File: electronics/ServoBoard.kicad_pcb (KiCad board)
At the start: 2 copper layers, 8 parts, among them K1 Left Servo, K2 Right Servo, P1 Pi GPIO Header, P2 CONN_2, U1 7805

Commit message: Gerber Files
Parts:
- added P3: CONNECTOR, 1pin, F.Cu at (40.6, 67.3)
- added P4: CONNECTOR, 1pin, F.Cu at (95.2, 111.8)
- added P5: CONNECTOR, 1pin, F.Cu at (40.6, 111.8)
- P2: footprint 2PIN_6mm -> PINHEAD1-2
- moved R1 36.9 mm to (40.6, 99.1), turned to 90 degrees
- moved C1 33.1 mm to (63.5, 96.5), turned to 270 degrees
- moved D1 23.3 mm to (40.6, 91.4), turned to 90 degrees
- moved K2 21.8 mm to (59.7, 110.5)
- moved K1 18.5 mm to (49.5, 110.5)
- moved P2 18.0 mm to (40.6, 85.1)
- moved P1 5.68 mm to (68.6, 68.6)
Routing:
- net N-0000033: track 0.00 -> 57.8 mm, vias 0 -> 4
- net N-000006: track 0.00 -> 42.7 mm
- net N-000008: track 0.00 -> 40.6 mm
- added copper zone on B.Cu, net +6V
- added copper zone on F.Cu, net GND
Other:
- board outline added: 59.7 x 49.5 mm
- board text added: "TurtleBot ServoBoard v0.1"

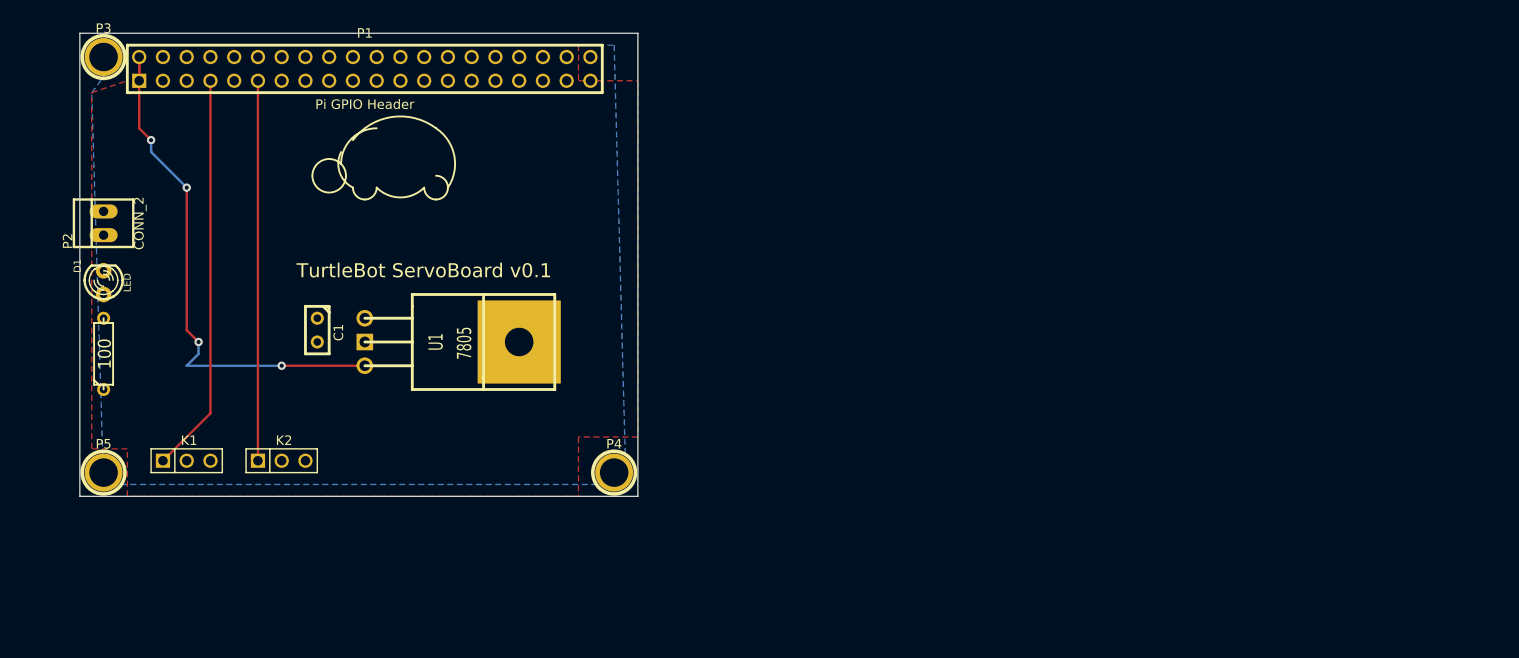
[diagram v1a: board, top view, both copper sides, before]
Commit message: Updated to be 5.6 x 6.5cm in width/length.
Moved pins to be over correct location.
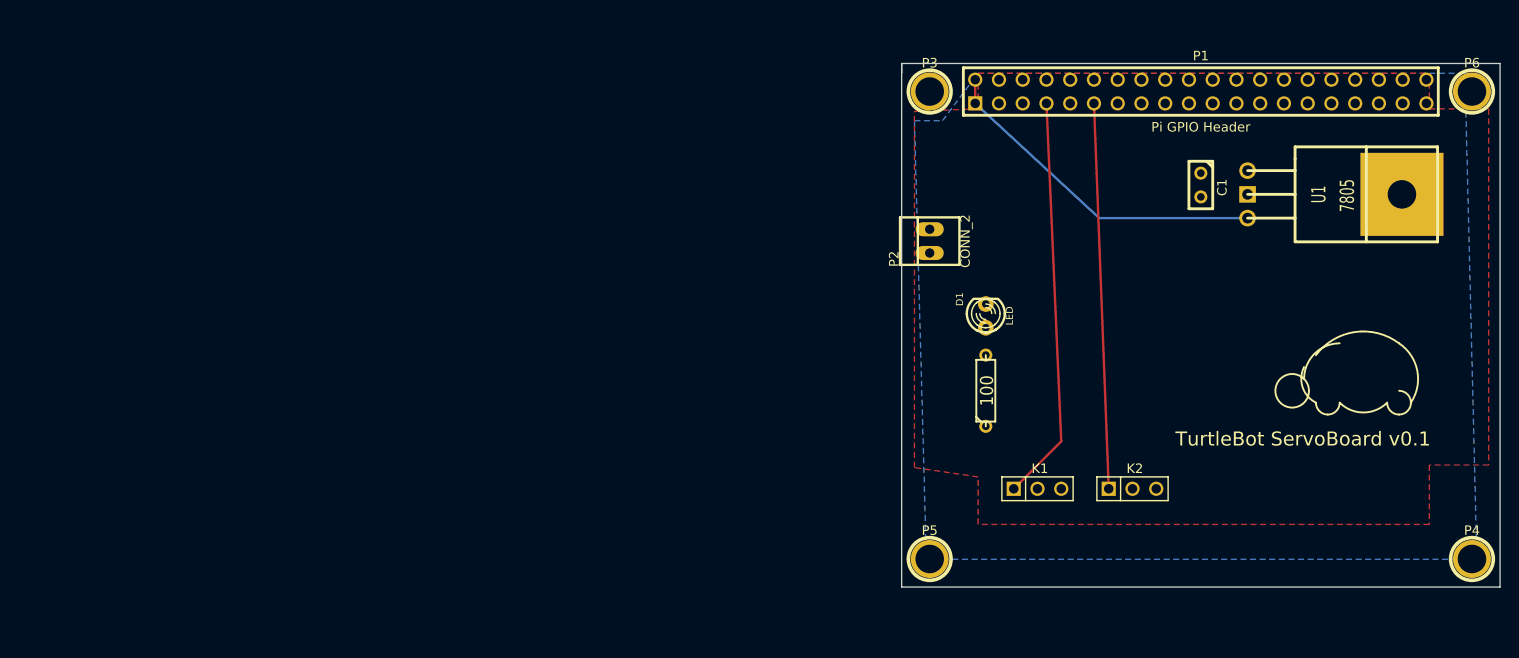
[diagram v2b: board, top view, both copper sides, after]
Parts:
- added P6: CONNECTOR, 1pin, F.Cu at (187.0, 71.0)
- moved C1 95.8 mm to (158.0, 81.0)
- moved U1 95.7 mm to (163.0, 82.0)
- moved R1 94.4 mm to (135.0, 103.0)
- moved D1 94.4 mm to (135.0, 95.0)
- moved P4 92.2 mm to (187.0, 121.0)
- moved K1 91.0 mm to (140.5, 113.5)
- moved K2 91.0 mm to (150.7, 113.5)
- moved P1 89.5 mm to (158.0, 71.0)
- moved P5 88.8 mm to (129.0, 121.0)
- moved P3 88.4 mm to (129.0, 71.0)
- moved P2 88.4 mm to (129.0, 87.0)
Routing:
- net N-0000033: track 57.8 -> 36.5 mm, vias 4 -> 0
- net N-000006: track 42.7 -> 43.4 mm
- net N-000008: track 40.6 -> 41.3 mm
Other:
- board size 59.7 x 49.5 mm -> 64 x 56 mm
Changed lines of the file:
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@@
     (links 16)
     (no_connects 1)
-    (area 35.179 63.373 100.711 115.443)
+    (area 123.539 66.29084 193.461 124.683)
     (thickness 1.6)
-    (drawings 16)
-    (tracks 18)
+    (drawings 18)
+    (tracks 6)
     (zones 0)
-    (modules 11)
+    (modules 12)
     (nets 7)
   )
@@
   )
   (module R3 (layer F.Cu)
-    (at 40.64 99.06 90)
+    (at 135 103 90)
     (descr "Resitance 3 pas")
     (tags R)
@@
   )
   (module PIN_ARRAY_20X2 (layer F.Cu)
-    (at 68.58 68.58)
+    (at 158 71)
     (descr "Double rangee de contacts 2 x 12 pins")
     (tags CONN)
@@
   )
   (module LM78XX (layer F.Cu)
-    (at 68.58 97.79)
+    (at 163 82)
     (descr "Regulateur TO220 serie LM78xx")
     (tags "TR TO220")
@@
   )
   (module LED-3MM (layer F.Cu)
-    (at 40.64 91.44 90)
+    (at 135 95 90)
     (descr "LED 3mm - Lead pitch 100mil (2,54mm)")
     (tags "LED led 3mm 3MM 100mil 2,54mm")
@@
   )
   (module C1 (layer F.Cu)
-    (at 63.5 96.52 270)
+    (at 158 81 270)
     (descr "Condensateur e = 1 pas")
     (tags C)
@@
   )
   (module PIN_ARRAY_3X1 (layer F.Cu)
-    (at 49.53 110.49)
+    (at 140.53 113.49)
     (descr "Connecteur 3 pins")
     (tags "CONN DEV")
@@
   )
   (module PIN_ARRAY_3X1 (layer F.Cu)
-    (at 59.69 110.49)
+    (at 150.69 113.49)
     (descr "Connecteur 3 pins")
     (tags "CONN DEV")
@@
   )
   (module 1pin (layer F.Cu)
-    (at 40.64 67.31)
+    (at 129 71)
     (descr "module 1 pin (ou trou mecanique de percage)")
     (tags DEV)
@@
   )
   (module 1pin (layer F.Cu)
-    (at 40.64 111.76)
+    (at 129 121)
     (descr "module 1 pin (ou trou mecanique de percage)")
     (tags DEV)
@@
   )
   (module 1pin (layer F.Cu)
-    (at 95.25 111.76)
+    (at 187 121)
     (descr "module 1 pin (ou trou mecanique de percage)")
     (tags DEV)
@@
   )
   (module PINHEAD1-2 (layer F.Cu)
-    (at 40.64 85.09 90)
+    (at 129 87 90)
     (attr virtual)
     (fp_text reference P2 (at -1.905 -3.81 90) (layer F.SilkS)
@@
     )
   )
-  (gr_arc (start 68.58 78.74) (end 67.31 81.28) (angle 90) (layer F.SilkS) (width 0.2))
-  (gr_arc (start 68.58 81.28) (end 68.58 82.55) (angle 90) (layer F.SilkS) (width 0.2))
-  (gr_arc (start 68.58 81.28) (end 69.85 81.28) (angle 90) (layer F.SilkS) (width 0.2))
-  (gr_arc (start 72.39 78.74) (end 74.93 81.28) (angle 90) (layer F.SilkS) (width 0.2))
-  (gr_arc (start 76.2 81.28) (end 76.2 82.55) (angle 90) (layer F.SilkS) (width 0.2))
-  (gr_arc (start 76.2 81.28) (end 77.47 81.28) (angle 90) (layer F.SilkS) (width 0.2))
-  (gr_arc (start 76.2 81.28) (end 76.2 80.01) (angle 90) (layer F.SilkS) (width 0.2))
-  (gr_arc (start 73.66 78.74) (end 76.2 74.93) (angle 90) (layer F.SilkS) (width 0.2))
-  (gr_arc (start 69.85 78.74) (end 66.04 78.74) (angle 90) (layer F.SilkS) (width 0.2))
-  (gr_arc (start 72.39 80.01) (end 67.31 76.2) (angle 90) (layer F.SilkS) (width 0.2))
-  (gr_circle (center 64.77 80.01) (end 66.04 81.28) (layer F.SilkS) (width 0.2))
-  (gr_text "TurtleBot ServoBoard v0.1" (at 74.93 90.17) (layer F.SilkS)
+  (module 1pin (layer F.Cu)
+    (at 187 71)
+    (descr "module 1 pin (ou trou mecanique de percage)")
+    (tags DEV)
+    (fp_text reference P6 (at 0 -3.048) (layer F.SilkS)
+      (effects (font (size 1.016 1.016) (thickness 0.254)))
+    )
+    (fp_text value CONNECTOR (at 0 2.794) (layer F.SilkS) hide
+      (effects (font (size 1.016 1.016) (thickness 0.254)))
+    )
+    (fp_circle (center 0 0) (end 0 -2.286) (layer F.SilkS) (width 0.381))
+    (pad 1 thru_hole circle (at 0 0) (size 4.064 4.064) (drill 3.048)
+      (layers *.Cu *.Mask F.SilkS)
+    )
+  )
+  (gr_line (start 190 124) (end 126 124) (angle 90) (layer Edge.Cuts) (width 0.1))
+  (gr_line (start 190 68) (end 126 68) (angle 90) (layer Edge.Cuts) (width 0.1))
+  (gr_line (start 190 124) (end 190 68) (angle 90) (layer Edge.Cuts) (width 0.1))
+  (gr_line (start 126 69) (end 126 68) (angle 90) (layer Edge.Cuts) (width 0.1))
+  (gr_line (start 126 68) (end 126 69) (angle 90) (layer Edge.Cuts) (width 0.1))
+  (gr_line (start 126 124) (end 126 69) (angle 90) (layer Edge.Cuts) (width 0.1))
+  (gr_arc (start 171.58 101.74) (end 170.31 104.28) (angle 90) (layer F.SilkS) (width 0.2))
+  (gr_arc (start 171.58 104.28) (end 171.58 105.55) (angle 90) (layer F.SilkS) (width 0.2))
+  (gr_arc (start 171.58 104.28) (end 172.85 104.28) (angle 90) (layer F.SilkS) (width 0.2))
+  (gr_arc (start 175.39 101.74) (end 177.93 104.28) (angle 90) (layer F.SilkS) (width 0.2))
+  (gr_arc (start 179.2 104.28) (end 179.2 105.55) (angle 90) (layer F.SilkS) (width 0.2))
+  (gr_arc (start 179.2 104.28) (end 180.47 104.28) (angle 90) (layer F.SilkS) (width 0.2))
+  (gr_arc (start 179.2 104.28) (end 179.2 103.01) (angle 90) (layer F.SilkS) (width 0.2))
+  (gr_arc (start 176.66 101.74) (end 179.2 97.93) (angle 90) (layer F.SilkS) (width 0.2))
+  (gr_arc (start 172.85 101.74) (end 169.04 101.74) (angle 90) (layer F.SilkS) (width 0.2))
+  (gr_arc (start 175.39 103.01) (end 170.31 99.2) (angle 90) (layer F.SilkS) (width 0.2))
+  (gr_circle (center 167.77 103.01) (end 169.04 104.28) (layer F.SilkS) (width 0.2))
+  (gr_text "TurtleBot ServoBoard v0.1" (at 168.93 108.17) (layer F.SilkS)
     (effects (font (size 1.5 1.5) (thickness 0.3)))
   )
-  (gr_line (start 38.1 114.3) (end 38.1 64.77) (angle 90) (layer Edge.Cuts) (width 0.1))
-  (gr_line (start 97.79 114.3) (end 38.1 114.3) (angle 90) (layer Edge.Cuts) (width 0.1))
-  (gr_line (start 97.79 64.77) (end 97.79 114.3) (angle 90) (layer Edge.Cuts) (width 0.1))
-  (gr_line (start 38.1 64.77) (end 97.79 64.77) (angle 90) (layer Edge.Cuts) (width 0.1))
-  (segment (start 44.45 69.85) (end 44.45 67.31) (width 0.254) (layer F.Cu) (net 4))
-  (segment (start 68.58 100.33) (end 59.69 100.33) (width 0.254) (layer F.Cu) (net 4))
-  (segment (start 44.45 74.93) (end 44.45 67.31) (width 0.254) (layer F.Cu) (net 4))
-  (segment (start 45.72 76.2) (end 44.45 74.93) (width 0.254) (layer F.Cu) (net 4))
-  (via (at 45.72 76.2) (size 0.889) (layers F.Cu B.Cu) (net 4))
-  (segment (start 45.72 77.47) (end 45.72 76.2) (width 0.254) (layer B.Cu) (net 4))
-  (segment (start 49.53 81.28) (end 45.72 77.47) (width 0.254) (layer B.Cu) (net 4))
-  (via (at 49.53 81.28) (size 0.889) (layers F.Cu B.Cu) (net 4))
-  (segment (start 49.53 96.52) (end 49.53 81.28) (width 0.254) (layer F.Cu) (net 4))
-  (segment (start 50.8 97.79) (end 49.53 96.52) (width 0.254) (layer F.Cu) (net 4))
-  (via (at 50.8 97.79) (size 0.889) (layers F.Cu B.Cu) (net 4))
-  (segment (start 50.8 99.06) (end 50.8 97.79) (width 0.254) (layer B.Cu) (net 4))
-  (segment (start 49.53 100.33) (end 50.8 99.06) (width 0.254) (layer B.Cu) (net 4))
-  (segment (start 59.69 100.33) (end 49.53 100.33) (width 0.254) (layer B.Cu) (net 4))
-  (via (at 59.69 100.33) (size 0.889) (layers F.Cu B.Cu) (net 4))
-  (segment (start 52.07 69.85) (end 52.07 105.41) (width 0.254) (layer F.Cu) (net 5))
-  (segment (start 52.07 105.41) (end 46.99 110.49) (width 0.254) (layer F.Cu) (net 5))
-  (segment (start 57.15 69.85) (end 57.15 110.49) (width 0.254) (layer F.Cu) (net 6))
+  (segment (start 163 84.54) (end 147.14 84.54) (width 0.254) (layer B.Cu) (net 4))
+  (segment (start 147.14 84.54) (end 133.87 72.27) (width 0.254) (layer B.Cu) (net 4) (status 20))
+  (segment (start 133.87 72.27) (end 133.87 69.73) (width 0.254) (layer F.Cu) (net 4) (status 30))
+  (segment (start 141.49 72.27) (end 143.07 108.41) (width 0.254) (layer F.Cu) (net 5) (status 10))
+  (segment (start 143.07 108.41) (end 137.99 113.49) (width 0.254) (layer F.Cu) (net 5))
+  (segment (start 146.57 72.27) (end 148.15 113.49) (width 0.254) (layer F.Cu) (net 6) (status 10))
   (zone (net 2) (net_name GND) (layer F.Cu) (hatch edge 0.508)
     (connect_pads (clearance 0.508))
@@
     (polygon
       (pts
-        (xy 97.79 107.95) (xy 91.44 107.95) (xy 91.44 114.3) (xy 43.18 114.3) (xy 43.18 109.22)
-        (xy 39.37 109.22) (xy 39.37 71.12) (xy 43.18 69.85) (xy 43.18 66.04) (xy 91.44 66.04)
-        (xy 91.44 69.85) (xy 97.79 69.85)
+        (xy 188.79 110.95) (xy 182.44 110.95) (xy 182.44 117.3) (xy 134.18 117.3) (xy 134.18 112.22)
+        (xy 127.37 111.22) (xy 127.37 73.12) (xy 134.18 72.85) (xy 134.18 69.04) (xy 182.44 69.04)
+        (xy 182.44 72.85) (xy 188.79 72.85)
       )
     )
@@
     (polygon
       (pts
-        (xy 39.37 71.12) (xy 43.18 66.04) (xy 95.25 66.04) (xy 96.52 113.03) (xy 40.64 113.03)
-        (xy 39.37 71.12)
+        (xy 130.37 74.12) (xy 134.18 69.04) (xy 186.25 69.04) (xy 187.52 121.03) (xy 128.64 121.03)
+        (xy 127.37 74.12)
       )
     )

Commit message: Added 2nd connector for power, may be a bit too small
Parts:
- added P7: CONN_2, PINHEAD1-2, F.Cu at (129.0, 80.0)
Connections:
- P2 pad 2: +6V -> N-0000031
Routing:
- net N-0000031: track 0.00 -> 4.46 mm
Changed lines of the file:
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@@
 (kicad_pcb (version 3) (host pcbnew "(2013-07-07 BZR 4022)-stable")
   (general
-    (links 16)
+    (links 17)
     (no_connects 1)
-    (area 123.539 66.29084 193.461 124.683)
+    (area 125.949999 67.949999 190.050001 124.050001)
     (thickness 1.6)
     (drawings 18)
-    (tracks 6)
+    (tracks 7)
     (zones 0)
-    (modules 12)
-    (nets 7)
+    (modules 13)
+    (nets 8)
   )
   (page USLetter)
@@
   )
   (setup
-    (last_trace_width 0.254)
+    (last_trace_width 1)
+    (user_trace_width 1)
     (trace_clearance 0.254)
     (zone_clearance 0.508)
@@
   (net 1 +6V)
   (net 2 GND)
-  (net 3 N-0000027)
-  (net 4 N-0000033)
-  (net 5 N-000006)
-  (net 6 N-000008)
+  (net 3 N-000001)
+  (net 4 N-0000027)
+  (net 5 N-0000031)
+  (net 6 N-0000034)
+  (net 7 N-000006)
   (net_class Default "This is the default net class."
     (clearance 0.254)
@@
     (add_net +6V)
     (add_net GND)
+    (add_net N-000001)
     (add_net N-0000027)
-    (add_net N-0000033)
+    (add_net N-0000031)
+    (add_net N-0000034)
     (add_net N-000006)
-    (add_net N-000008)
   )
   (module R3 (layer F.Cu)
@@
     (pad 2 thru_hole circle (at 3.81 0 90) (size 1.397 1.397) (drill 0.8128)
       (layers *.Cu *.Mask F.SilkS)
-      (net 3 N-0000027)
+      (net 4 N-0000027)
     )
     (model discret/resistor.wrl
@@
     (pad 1 thru_hole rect (at -24.13 1.27) (size 1.524 1.524) (drill 1.016)
       (layers *.Cu *.Mask F.SilkS)
-      (net 4 N-0000033)
+      (net 6 N-0000034)
     )
     (pad 2 thru_hole circle (at -24.13 -1.27) (size 1.524 1.524) (drill 1.016)
       (layers *.Cu *.Mask F.SilkS)
-      (net 4 N-0000033)
+      (net 6 N-0000034)
     )
     (pad 11 thru_hole circle (at -11.43 1.27) (size 1.524 1.524) (drill 1.016)
       (layers *.Cu *.Mask F.SilkS)
-      (net 6 N-000008)
+      (net 7 N-000006)
     )
     (pad 4 thru_hole circle (at -21.59 -1.27) (size 1.524 1.524) (drill 1.016)
@@
     (pad 7 thru_hole circle (at -16.51 1.27) (size 1.524 1.524) (drill 1.016)
       (layers *.Cu *.Mask F.SilkS)
-      (net 5 N-000006)
+      (net 3 N-000001)
     )
     (pad 9 thru_hole circle (at -13.97 1.27) (size 1.524 1.524) (drill 1.016)
@@
     (pad VO thru_hole circle (at 0 2.54) (size 1.778 1.778) (drill 1.143)
       (layers *.Cu *.Mask F.SilkS)
-      (net 4 N-0000033)
+      (net 6 N-0000034)
     )
     (model discret/to220_horiz.wrl
@@
     (pad 1 thru_hole circle (at -1.27 0 90) (size 1.6764 1.6764) (drill 0.8128)
       (layers *.Cu *.Mask F.SilkS)
-      (net 3 N-0000027)
+      (net 4 N-0000027)
     )
     (pad 2 thru_hole circle (at 1.27 0 90) (size 1.6764 1.6764) (drill 0.8128)
@@
     (pad 1 thru_hole rect (at -2.54 0) (size 1.524 1.524) (drill 1.016)
       (layers *.Cu *.Mask F.SilkS)
-      (net 5 N-000006)
+      (net 3 N-000001)
     )
     (pad 2 thru_hole circle (at 0 0) (size 1.524 1.524) (drill 1.016)
@@
     (pad 1 thru_hole rect (at -2.54 0) (size 1.524 1.524) (drill 1.016)
       (layers *.Cu *.Mask F.SilkS)
-      (net 6 N-000008)
+      (net 7 N-000006)
     )
     (pad 2 thru_hole circle (at 0 0) (size 1.524 1.524) (drill 1.016)
@@
     (pad 2 thru_hole oval (at 1.27 0 90) (size 1.50622 3.01498) (drill 0.99822)
       (layers *.Cu F.Paste F.SilkS F.Mask)
-      (net 1 +6V)
+      (net 5 N-0000031)
     )
   )
@@
     (pad 1 thru_hole circle (at 0 0) (size 4.064 4.064) (drill 3.048)
       (layers *.Cu *.Mask F.SilkS)
+    )
+  )
+  (module PINHEAD1-2 (layer F.Cu)
+    (at 129 80 90)
+    (attr virtual)
+    (fp_text reference P7 (at -1.905 -3.81 90) (layer F.SilkS)
+      (effects (font (size 1.016 1.016) (thickness 0.0889)))
+    )
+    (fp_text value CONN_2 (at 0 3.81 90) (layer F.SilkS)
+      (effects (font (size 1.016 1.016) (thickness 0.0889)))
+    )
+    (fp_line (start 2.54 -1.27) (end -2.54 -1.27) (layer F.SilkS) (width 0.254))
+    (fp_line (start 2.54 3.175) (end -2.54 3.175) (layer F.SilkS) (width 0.254))
+    (fp_line (start -2.54 -3.175) (end 2.54 -3.175) (layer F.SilkS) (width 0.254))
+    (fp_line (start -2.54 -3.175) (end -2.54 3.175) (layer F.SilkS) (width 0.254))
+    (fp_line (start 2.54 -3.175) (end 2.54 3.175) (layer F.SilkS) (width 0.254))
+    (pad 1 thru_hole oval (at -1.27 0 90) (size 1.50622 3.01498) (drill 0.99822)
+      (layers *.Cu F.Paste F.SilkS F.Mask)
+      (net 5 N-0000031)
+    )
+    (pad 2 thru_hole oval (at 1.27 0 90) (size 1.50622 3.01498) (drill 0.99822)
+      (layers *.Cu F.Paste F.SilkS F.Mask)
+      (net 1 +6V)
     )
   )
@@
     (effects (font (size 1.5 1.5) (thickness 0.3)))
   )
-  (segment (start 163 84.54) (end 147.14 84.54) (width 0.254) (layer B.Cu) (net 4))
-  (segment (start 147.14 84.54) (end 133.87 72.27) (width 0.254) (layer B.Cu) (net 4) (status 20))
-  (segment (start 133.87 72.27) (end 133.87 69.73) (width 0.254) (layer F.Cu) (net 4) (status 30))
-  (segment (start 141.49 72.27) (end 143.07 108.41) (width 0.254) (layer F.Cu) (net 5) (status 10))
-  (segment (start 143.07 108.41) (end 137.99 113.49) (width 0.254) (layer F.Cu) (net 5))
-  (segment (start 146.57 72.27) (end 148.15 113.49) (width 0.254) (layer F.Cu) (net 6) (status 10))
+  (segment (start 141.49 72.27) (end 143.07 108.41) (width 0.254) (layer F.Cu) (net 3) (status 10))
+  (segment (start 143.07 108.41) (end 137.99 113.49) (width 0.254) (layer F.Cu) (net 3))
+  (segment (start 129 81.27) (end 129 85.73) (width 1) (layer B.Cu) (net 5) (status C00000))
+  (segment (start 163 84.54) (end 147.14 84.54) (width 0.254) (layer B.Cu) (net 6))
+  (segment (start 147.14 84.54) (end 133.87 72.27) (width 0.254) (layer B.Cu) (net 6) (status 20))
+  (segment (start 133.87 72.27) (end 133.87 69.73) (width 0.254) (layer F.Cu) (net 6) (status 30))
+  (segment (start 146.57 72.27) (end 148.15 113.49) (width 0.254) (layer F.Cu) (net 7) (status 10))
   (zone (net 2) (net_name GND) (layer F.Cu) (hatch edge 0.508)
     (connect_pads (clearance 0.508))
